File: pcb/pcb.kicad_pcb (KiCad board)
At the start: 2 copper layers, 170.2 x 137.2 mm, 169 parts, among them J1 Barrel_Jack, J10 Screw_Terminal_01x08, J11 Conn_01x08_Male, J12 Conn_01x08_Male, J13 Conn_01x08_Male, J14 Conn_01x08_Male, J2 Barrel_Jack, J3 Screw_Terminal_01x03, J4 Screw_Terminal_01x02, J5 Conn_02x05_Odd_Even, J6 Conn_01x06_Male, J7 Screw_Terminal_01x08, J8 Screw_Terminal_01x08, J9 Screw_Terminal_01x08, SW1 SW_SPDT, U1 CPC5001G, U10 LTV-847, U11 LTV-847, U12 MCP23017-E_SP, U13 MCP23017-E_SP, U2 MCP23017-E_SP, U3 LTV-847, U4 LTV-847, U5 LTV-847, U6 LTV-847, U7 MCP23017-E_SP, U8 LTV-847, U9 LTV-847

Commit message: update
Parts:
- D33, D34, D35, D36, D37, D38, D39, D40, D41, D42, D43, D44, D45, D46, D47, D48, D49, D50, D51, D52, D53, D54, D55, D56, D57, D58, D59, D60, D61, D62, D63, D64: value LED 2mA -> RED
- H1, H2, H3, H4: footprint MountingHole:MountingHole_4.3mm_M4 -> MountingHole:MountingHole_3.2mm_M3
- moved R65 24.1 mm to (98.4, 92.1)
- moved C1 24.1 mm to (102.2, 95.2)
- moved C2 24.1 mm to (116.2, 94.6)
- moved R66 24.1 mm to (120.0, 85.7)
- moved U1 24.1 mm to (105.4, 89.5)
- moved J6 24.1 mm to (93.3, 78.7)
- moved SW1 23.8 mm to (103.6, 59.1)
- moved A1 23.8 mm to (136.5, 64.1)
- moved J5 21.0 mm to (87.6, 88.9)
- moved J3 17.8 mm to (96.5, 24.1)
- moved J14 15.9 mm to (127.6, 24.1)
- moved C5 14.9 mm to (155.2, 82.9)
- moved U2 14.9 mm to (152.0, 103.2)
- moved C6 13.3 mm to (156.2, 69.8)
- moved U13 13.3 mm to (159.4, 49.5)
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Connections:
- A1 pad 10: /~RESET_IN2 -> /~RESET_OUT2
- A1 pad 12: /~RESET_OUT2 -> /~RESET_IN2
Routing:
- net +12V: track 0.00 -> 361.4 mm
- net +5V: track 0.00 -> 265.3 mm, vias 0 -> 2
- net SDA: track 0.00 -> 118.7 mm, vias 0 -> 3
- net /~RESET_IN2: track 0.00 -> 113.8 mm, vias 0 -> 4
- net /INTB2: track 0.00 -> 108.9 mm, vias 0 -> 4
- net /INTA2: track 0.00 -> 105.4 mm, vias 0 -> 4
- net /~RESET_OUT1: track 0.00 -> 105.0 mm, vias 0 -> 3
- net SCL: track 0.00 -> 104.1 mm, vias 0 -> 3
- net /Output 2/Out15: track 0.00 -> 100.5 mm
- net +9V: track 0.00 -> 91.7 mm
- net /Output 2/Out14: track 0.00 -> 90.9 mm
- net /Output 2/Out13: track 0.00 -> 82.2 mm
- net /Output 1/Out0: track 0.00 -> 80.5 mm
- net /Output 2/Out12: track 0.00 -> 76.2 mm
- net /Output 1/Out1: track 0.00 -> 73.3 mm
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- added copper zone on B.Cu, net /GNDcomm
- added copper zone on B.Cu, net GND
- added copper zone on B.Cu, net GNDD
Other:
- net class Default: clearance 0.15 -> 0.254; trace_width 0.25 -> 0.381
- net class Power: clearance 0.25 -> 0.254; trace_width 0.35 -> 0.762
- rule trace_clearance: 0.15 -> 0.254
- rule trace_min: 0.15 -> 0.1524
- board text added: "BLK"
- board text added: "GRN"
- board text removed: "black"
- board text removed: "green"

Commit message: Update
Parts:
- C1, C2: value 22pF -> 0.1uF
- H1, H2, H3, H4: footprint MountingHole:MountingHole_3.2mm_M3 -> MountingHole:MountingHole_4.3mm_M4
- R65, R66: value 470 -> 1k
- moved C1 2.54 mm to (102.2, 92.7), turned to 270 degrees
- moved C2 2.50 mm to (116.2, 92.1), turned to 270 degrees
- moved J2 1.91 mm to (99.1, 143.5)
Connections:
- C1 pad 1: /Vcomm -> /GNDcomm
- C1 pad 2: /GNDcomm -> /Vcomm
- C2 pad 1: GND -> +5V
- C2 pad 2: +5V -> GND
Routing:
- net /Output 2/Out7: track 55.9 -> 39.8 mm
- net /Output 2/Out6: track 59.9 -> 54.0 mm
- net /Output 1/Out5: track 40.9 -> 46.0 mm
- net /Output 1/Out3: track 55.2 -> 60.4 mm
- net /Output 1/Out4: track 48.1 -> 53.2 mm
- net /Output 1/Out0: track 80.5 -> 85.3 mm
- net /Output 1/Out2: track 64.0 -> 68.8 mm
- net +12V: track 361.4 -> 356.8 mm
- net /Output 1/Out1: track 73.3 -> 77.5 mm
- net /Output 1/Out6: track 34.9 -> 39.0 mm
- net /Input 2/Pin15: track 19.9 -> 23.6 mm
- net /Output 1/Out8: track 36.6 -> 39.9 mm
- net /Input 1/Pin4: track 28.9 -> 32.3 mm
- net /Input 1/Pin5: track 26.4 -> 29.0 mm
- net /Input 1/Pin1: track 40.3 -> 38.0 mm
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
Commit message: latest
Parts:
- R1, R10, R11, R12, R13, R14, R15, R16, R17, R18, R19, R2, R20, R21, R22, R23, R24, R25, R26, R27, R28, R29, R3, R30, R31, R32, R4, R5, R6, R7, R8, R9: value 680 1W -> 1k 1W
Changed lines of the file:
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@@
-(kicad_pcb (version 20171130) (host pcbnew 5.0.2)
+(kicad_pcb (version 20171130) (host pcbnew 5.0.2-1.fc29)
   (general
     (thickness 1.6)
@@
       (effects (font (size 1 1) (thickness 0.15)))
     )
-    (fp_text value "680 1W" (at 2.54 3.37 270) (layer F.Fab)
+    (fp_text value "1k 1W" (at 2.54 3.37 270) (layer F.Fab)
       (effects (font (size 1 1) (thickness 0.15)))
     )
@@
       (effects (font (size 1 1) (thickness 0.15)))
     )
-    (fp_text value "680 1W" (at 2.54 3.37 270) (layer F.Fab)
+    (fp_text value "1k 1W" (at 2.54 3.37 270) (layer F.Fab)
       (effects (font (size 1 1) (thickness 0.15)))
     )
@@
       (effects (font (size 1 1) (thickness 0.15)))
     )
-    (fp_text value "680 1W" (at 2.54 3.37 270) (layer F.Fab)
+    (fp_text value "1k 1W" (at 2.54 3.37 270) (layer F.Fab)
       (effects (font (size 1 1) (thickness 0.15)))
     )
@@
       (effects (font (size 1 1) (thickness 0.15)))
     )
-    (fp_text value "680 1W" (at 2.54 3.37 270) (layer F.Fab)
+    (fp_text value "1k 1W" (at 2.54 3.37 270) (layer F.Fab)
       (effects (font (size 1 1) (thickness 0.15)))
     )
@@
       (effects (font (size 1 1) (thickness 0.15)))
     )
-    (fp_text value "680 1W" (at 2.54 3.37 270) (layer F.Fab)
+    (fp_text value "1k 1W" (at 2.54 3.37 270) (layer F.Fab)
       (effects (font (size 1 1) (thickness 0.15)))
     )
@@
       (effects (font (size 1 1) (thickness 0.15)))
     )
-    (fp_text value "680 1W" (at 2.54 3.37 270) (layer F.Fab)
+    (fp_text value "1k 1W" (at 2.54 3.37 270) (layer F.Fab)
       (effects (font (size 1 1) (thickness 0.15)))
     )
@@
       (effects (font (size 1 1) (thickness 0.15)))
     )
-    (fp_text value "680 1W" (at 2.54 3.37 270) (layer F.Fab)
+    (fp_text value "1k 1W" (at 2.54 3.37 270) (layer F.Fab)
       (effects (font (size 1 1) (thickness 0.15)))
     )
@@
       (effects (font (size 1 1) (thickness 0.15)))
     )
-    (fp_text value "680 1W" (at 2.54 3.37 270) (layer F.Fab)
+    (fp_text value "1k 1W" (at 2.54 3.37 270) (layer F.Fab)
       (effects (font (size 1 1) (thickness 0.15)))
     )
@@
       (effects (font (size 1 1) (thickness 0.15)))
     )
-    (fp_text value "680 1W" (at 2.54 3.37 270) (layer F.Fab)
+    (fp_text value "1k 1W" (at 2.54 3.37 270) (layer F.Fab)
       (effects (font (size 1 1) (thickness 0.15)))
     )
@@
       (effects (font (size 1 1) (thickness 0.15)))
     )
-    (fp_text value "680 1W" (at 2.54 3.37 270) (layer F.Fab)
+    (fp_text value "1k 1W" (at 2.54 3.37 270) (layer F.Fab)
       (effects (font (size 1 1) (thickness 0.15)))
     )
@@
       (effects (font (size 1 1) (thickness 0.15)))
     )
-    (fp_text value "680 1W" (at 2.54 3.37 270) (layer F.Fab)
+    (fp_text value "1k 1W" (at 2.54 3.37 270) (layer F.Fab)
       (effects (font (size 1 1) (thickness 0.15)))
     )
@@
       (effects (font (size 1 1) (thickness 0.15)))
     )
-    (fp_text value "680 1W" (at 2.54 3.37 270) (layer F.Fab)
+    (fp_text value "1k 1W" (at 2.54 3.37 270) (layer F.Fab)
       (effects (font (size 1 1) (thickness 0.15)))
     )
@@
       (effects (font (size 1 1) (thickness 0.15)))
     )
-    (fp_text value "680 1W" (at 2.54 3.37 270) (layer F.Fab)
+    (fp_text value "1k 1W" (at 2.54 3.37 270) (layer F.Fab)
       (effects (font (size 1 1) (thickness 0.15)))
     )
@@
       (effects (font (size 1 1) (thickness 0.15)))
     )
-    (fp_text value "680 1W" (at 2.54 3.37 270) (layer F.Fab)
+    (fp_text value "1k 1W" (at 2.54 3.37 270) (layer F.Fab)
       (effects (font (size 1 1) (thickness 0.15)))
     )
@@
       (effects (font (size 1 1) (thickness 0.15)))
     )
-    (fp_text value "680 1W" (at 2.54 3.37 270) (layer F.Fab)
+    (fp_text value "1k 1W" (at 2.54 3.37 270) (layer F.Fab)
       (effects (font (size 1 1) (thickness 0.15)))
     )
@@
       (effects (font (size 1 1) (thickness 0.15)))
     )
-    (fp_text value "680 1W" (at 2.54 3.37 270) (layer F.Fab)
+    (fp_text value "1k 1W" (at 2.54 3.37 270) (layer F.Fab)
       (effects (font (size 1 1) (thickness 0.15)))
     )
@@
       (effects (font (size 1 1) (thickness 0.15)))
     )
-    (fp_text value "680 1W" (at 2.54 3.37 270) (layer F.Fab)
+    (fp_text value "1k 1W" (at 2.54 3.37 270) (layer F.Fab)
       (effects (font (size 1 1) (thickness 0.15)))
     )
@@
       (effects (font (size 1 1) (thickness 0.15)))
     )
-    (fp_text value "680 1W" (at 2.54 3.37 270) (layer F.Fab)
+    (fp_text value "1k 1W" (at 2.54 3.37 270) (layer F.Fab)
       (effects (font (size 1 1) (thickness 0.15)))
     )
@@
       (effects (font (size 1 1) (thickness 0.15)))
     )
-    (fp_text value "680 1W" (at 2.54 3.37 270) (layer F.Fab)
+    (fp_text value "1k 1W" (at 2.54 3.37 270) (layer F.Fab)
       (effects (font (size 1 1) (thickness 0.15)))
     )
@@
       (effects (font (size 1 1) (thickness 0.15)))
     )
-    (fp_text value "680 1W" (at 2.54 3.37 270) (layer F.Fab)
+    (fp_text value "1k 1W" (at 2.54 3.37 270) (layer F.Fab)
       (effects (font (size 1 1) (thickness 0.15)))
     )
@@
       (effects (font (size 1 1) (thickness 0.15)))
     )
-    (fp_text value "680 1W" (at 2.54 3.37 270) (layer F.Fab)
+    (fp_text value "1k 1W" (at 2.54 3.37 270) (layer F.Fab)
       (effects (font (size 1 1) (thickness 0.15)))
     )
@@
       (effects (font (size 1 1) (thickness 0.15)))
     )
-    (fp_text value "680 1W" (at 2.54 3.37 270) (layer F.Fab)
+    (fp_text value "1k 1W" (at 2.54 3.37 270) (layer F.Fab)
       (effects (font (size 1 1) (thickness 0.15)))
     )
@@
       (effects (font (size 1 1) (thickness 0.15)))
     )
-    (fp_text value "680 1W" (at 2.54 3.37 270) (layer F.Fab)
+    (fp_text value "1k 1W" (at 2.54 3.37 270) (layer F.Fab)
       (effects (font (size 1 1) (thickness 0.15)))
     )
@@
       (effects (font (size 1 1) (thickness 0.15)))
     )
-    (fp_text value "680 1W" (at 2.54 3.37 270) (layer F.Fab)
+    (fp_text value "1k 1W" (at 2.54 3.37 270) (layer F.Fab)
       (effects (font (size 1 1) (thickness 0.15)))
     )
@@
       (effects (font (size 1 1) (thickness 0.15)))
     )
-    (fp_text value "680 1W" (at 2.54 3.37 270) (layer F.Fab)
+    (fp_text value "1k 1W" (at 2.54 3.37 270) (layer F.Fab)
       (effects (font (size 1 1) (thickness 0.15)))
     )
@@
       (effects (font (size 1 1) (thickness 0.15)))
     )
-    (fp_text value "680 1W" (at 2.54 3.37 270) (layer F.Fab)
+    (fp_text value "1k 1W" (at 2.54 3.37 270) (layer F.Fab)
       (effects (font (size 1 1) (thickness 0.15)))
     )
@@
       (effects (font (size 1 1) (thickness 0.15)))
     )
-    (fp_text value "680 1W" (at 2.54 3.37 270) (layer F.Fab)
+    (fp_text value "1k 1W" (at 2.54 3.37 270) (layer F.Fab)
       (effects (font (size 1 1) (thickness 0.15)))
     )
@@
       (effects (font (size 1 1) (thickness 0.15)))
     )
-    (fp_text value "680 1W" (at 2.54 3.37 270) (layer F.Fab)
+    (fp_text value "1k 1W" (at 2.54 3.37 270) (layer F.Fab)
       (effects (font (size 1 1) (thickness 0.15)))
     )
@@
       (effects (font (size 1 1) (thickness 0.15)))
     )
-    (fp_text value "680 1W" (at 2.54 3.37 270) (layer F.Fab)
+    (fp_text value "1k 1W" (at 2.54 3.37 270) (layer F.Fab)
       (effects (font (size 1 1) (thickness 0.15)))
     )
@@
       (effects (font (size 1 1) (thickness 0.15)))
     )
-    (fp_text value "680 1W" (at 2.54 3.37 270) (layer F.Fab)
+    (fp_text value "1k 1W" (at 2.54 3.37 270) (layer F.Fab)
       (effects (font (size 1 1) (thickness 0.15)))
     )
@@
       (effects (font (size 1 1) (thickness 0.15)))
     )
-    (fp_text value "680 1W" (at 2.54 3.37 270) (layer F.Fab)
+    (fp_text value "1k 1W" (at 2.54 3.37 270) (layer F.Fab)
       (effects (font (size 1 1) (thickness 0.15)))
     )
@@
       (effects (font (size 1 1) (thickness 0.15)))
     )
-    (fp_text value "680 1W" (at 2.54 3.37 270) (layer F.Fab)
+    (fp_text value "1k 1W" (at 2.54 3.37 270) (layer F.Fab)
       (effects (font (size 1 1) (thickness 0.15)))
     )

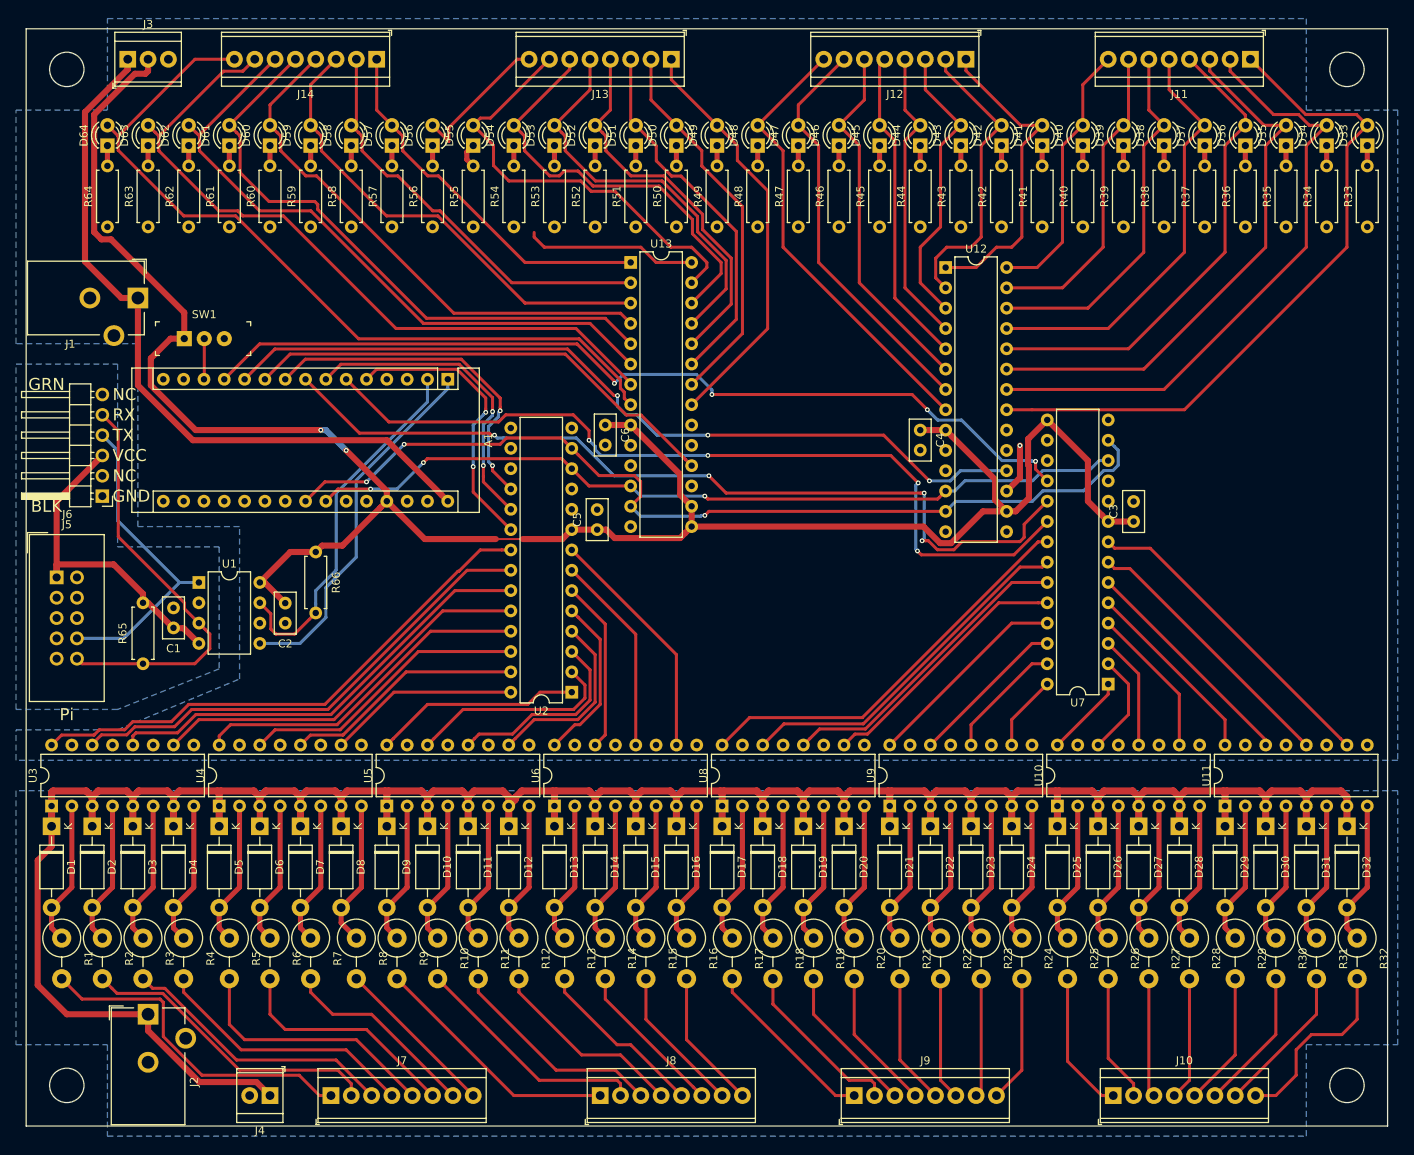
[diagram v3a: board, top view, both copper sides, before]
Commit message: 4 layer PCB
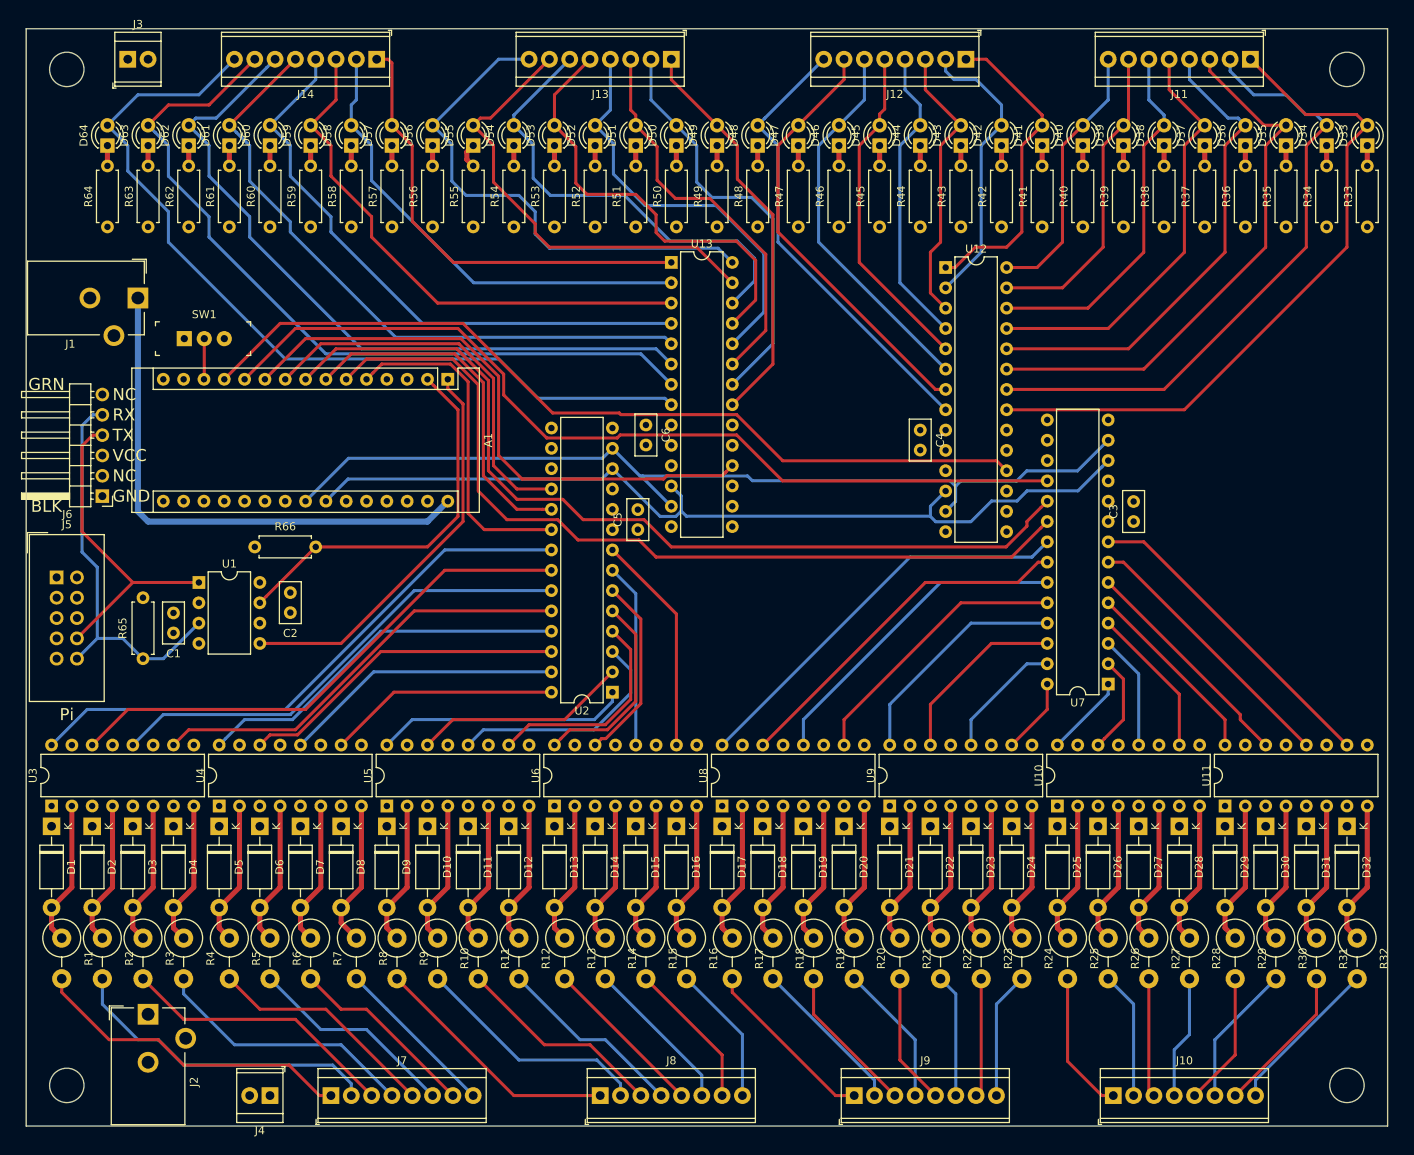
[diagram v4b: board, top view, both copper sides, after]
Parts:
- J3: value Screw_Terminal_01x03 -> Screw_Terminal_01x02; footprint TerminalBlock_TE-Connectivity:TerminalBlock_TE_282834-3_1x03_P2.54mm_Horizontal -> TerminalBlock_TE-Connectivity:TerminalBlock_TE_282834-2_1x02_P2.54mm_Horizontal
- moved R66 7.65 mm to (112.4, 85.1), turned to 0 degrees
- moved U13 5.08 mm to (164.5, 49.5)
- moved U2 5.08 mm to (157.1, 103.2)
- moved C5 5.08 mm to (160.3, 82.9)
- moved C6 5.08 mm to (161.3, 69.8)
- moved C2 1.46 mm to (116.8, 90.8)
- moved C1 0.64 mm to (102.2, 93.3)
- moved R65 0.64 mm to (98.4, 91.4)
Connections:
- A1 pad 11: /~RESET_OUT1 -> /~RESET_IN2
- A1 pad 12: /~RESET_IN2 -> /~RESET_OUT1
- J3 pad 1: +9V -> +5V
- J3 pad 2: +5V -> GND
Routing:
- net +12V: track 356.8 -> 0.00 mm
- net +5V: track 265.3 -> 0.00 mm, vias 2 -> 0
- net /Vcomm: track 41.8 -> 0.00 mm
- net +9V: track 91.7 -> 67.0 mm
- net /Output 2/Out7: track 39.8 -> 64.4 mm
- net /~RESET_OUT2: track 60.4 -> 74.3 mm
- net /Output 2/Out8: track 47.1 -> 57.5 mm
- net SCL: track 104.1 -> 113.6 mm, vias 3 -> 0
- net /Output 2/Out14: track 90.9 -> 99.3 mm
- net /Output 2/Out13: track 82.2 -> 90.6 mm
- net /Output 2/Out15: track 100.5 -> 108.3 mm
- net /Output 2/Out10: track 59.9 -> 67.6 mm
- net /Output 2/Out11: track 67.0 -> 74.4 mm
- net /Output 2/Out9: track 52.7 -> 59.2 mm
- net GND: track 6.77 -> 0.38 mm, vias 1 -> 0
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- added copper zone on In1.Cu, net +12V
- added copper zone on In1.Cu, net +5V
- added copper zone on In2.Cu, net /GNDcomm
- added copper zone on In1.Cu, net /Vcomm
- added copper zone on In2.Cu, net GND
- added copper zone on In2.Cu, net GNDD
- removed copper zone on B.Cu, net /GNDcomm
- removed copper zone on B.Cu, net GND
- removed copper zone on B.Cu, net GNDD
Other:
- copper layers 2 -> 4

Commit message: stuff
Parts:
- added R67: 4.7k, Resistor_THT:R_Axial_DIN0207_L6.3mm_D2.5mm_P7.62mm_Horizontal, F.Cu at (118.1, 66.7)
- added R68: 4.7k, Resistor_THT:R_Axial_DIN0207_L6.3mm_D2.5mm_P7.62mm_Horizontal, F.Cu at (121.3, 66.7)
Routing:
- net /RX: track 48.0 -> 36.6 mm
- net SDA: track 116.3 -> 121.7 mm
- net SCL: track 113.6 -> 118.6 mm
- net /TX: track 50.3 -> 45.7 mm
- net /Output 1/Out0: track 85.3 -> 86.9 mm
- net /Output 1/Out2: track 68.8 -> 67.9 mm
- net /Output 1/Out3: track 61.1 -> 60.4 mm
- net /INTA1: track 42.1 -> 42.8 mm
